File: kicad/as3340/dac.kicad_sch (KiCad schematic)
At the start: 29 parts, among them U14 AD5328, U2 LM4040AIM3-2.5, U5 TL074

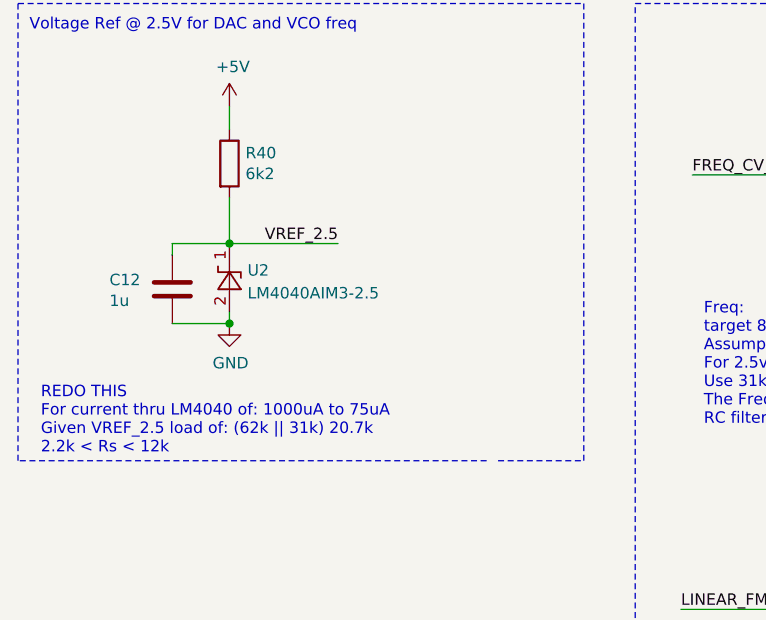
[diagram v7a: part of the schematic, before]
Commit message: some routing modifications and updated JLCPCB parts list
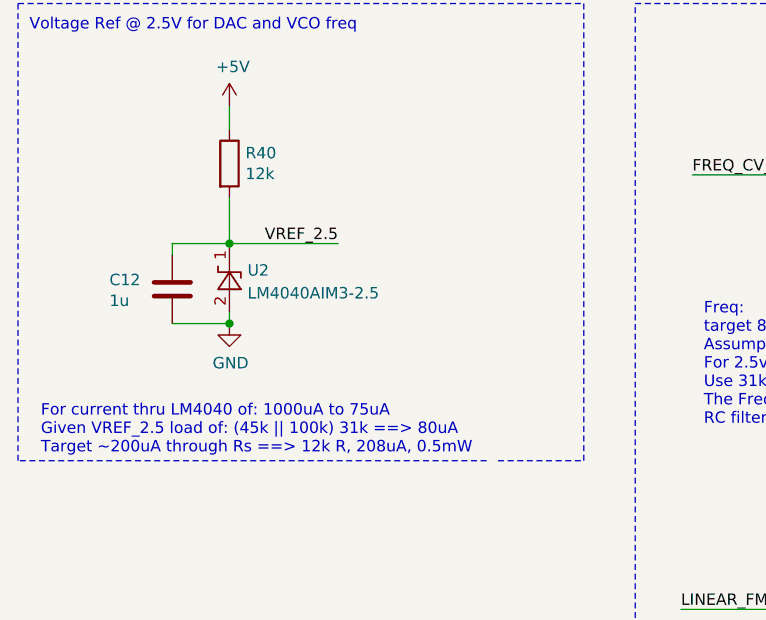
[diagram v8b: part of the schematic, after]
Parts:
- C16: LCSC Part C2761748 -> C21122
- C3: LCSC Part (none) -> C1588
- C36: LCSC Part (none) -> C53987
- R38, R39: LCSC Part (none) -> C25803
- R40: value 6k2 -> 12k; footprint Resistor_SMD:R_1206_3216Metric -> Resistor_SMD:R_0603_1608Metric; LCSC Part (none) -> C22790
- R50: LCSC Part (none) -> C21190
- R61: LCSC Part (none) -> C4216
- R64: LCSC Part (none) -> C23196
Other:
- note added: "For current thru LM4040 of: 1000uA to 75uA Given VREF_2.5 load of: (45k || 100k) 31k ==> 80uA Target ~200uA through Rs ==> 12k R, 208uA, 0.5mW"
- note removed: "REDO THIS For current thru LM4040 of: 1000uA to 75uA Given VREF_2.5 load of: (62k || 31k) 20.7k 2.2k < Rs < 12k"
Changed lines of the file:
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@@
   (title_block
     (title "Zoxnoxious 3340 Oscillator")
-    (rev "0.4")
+    (date "2024-06-20")
+    (rev "0.7")
     (company "Zoxnoxious Engineering")
   )
@@
     (effects (font (size 1.27 1.27)) (justify left bottom))
   )
-  (text "REDO THIS\nFor current thru LM4040 of: 1000uA to 75uA\nGiven VREF_2.5 load of: (62k || 31k) 20.7k\n2.2k < Rs < 12k\n"
+  (text "For current thru LM4040 of: 1000uA to 75uA\nGiven VREF_2.5 load of: (45k || 100k) 31k ==> 80uA\nTarget ~200uA through Rs ==> 12k R, 208uA, 0.5mW\n"
     (at 20.32 168.275 0)
     (effects (font (size 1.27 1.27)) (justify left bottom))
@@
       (effects (font (size 1.27 1.27)) hide)
     )
-    (property "LCSC Part" "" (at 118.11 137.16 0)
+    (property "LCSC Part" "C21190" (at 118.11 137.16 0)
       (effects (font (size 1.27 1.27)) hide)
     )
@@
       (effects (font (size 1.27 1.27)) hide)
     )
-    (property "LCSC Part" "" (at 245.11 58.42 0)
+    (property "LCSC Part" "C4216" (at 245.11 58.42 0)
       (effects (font (size 1.27 1.27)) hide)
     )
@@
       (effects (font (size 1.27 1.27)) hide)
     )
-    (property "LCSC Part" "" (at 261.62 52.07 0)
+    (property "LCSC Part" "C23196" (at 261.62 52.07 0)
       (effects (font (size 1.27 1.27)) hide)
     )
@@
       (effects (font (size 1.27 1.27)) hide)
     )
-    (property "LCSC Part" "" (at 332.74 58.42 0)
+    (property "LCSC Part" "C25803" (at 332.74 58.42 0)
       (effects (font (size 1.27 1.27)) hide)
     )
@@
       (effects (font (size 1.27 1.27)) (justify left))
     )
-    (property "Value" "6k2" (at 43.053 137.033 0)
+    (property "Value" "12k" (at 43.053 137.033 0)
       (effects (font (size 1.27 1.27)) (justify left))
     )
-    (property "Footprint" "Resistor_SMD:R_1206_3216Metric" (at 39.497 135.89 90)
+    (property "Footprint" "Resistor_SMD:R_0603_1608Metric" (at 39.497 135.89 90)
       (effects (font (size 1.27 1.27)) hide)
     )
@@
       (effects (font (size 1.27 1.27)) hide)
     )
-    (property "LCSC Part" "" (at 41.275 135.89 0)
+    (property "LCSC Part" "C22790" (at 41.275 135.89 0)
       (effects (font (size 1.27 1.27)) hide)
     )
@@
       (effects (font (size 1.27 1.27)) hide)
     )
-    (property "LCSC Part" "" (at 349.25 52.07 0)
+    (property "LCSC Part" "C25803" (at 349.25 52.07 0)
       (effects (font (size 1.27 1.27)) hide)
     )
@@
       (effects (font (size 1.27 1.27)) hide)
     )
-    (property "LCSC Part" "" (at 349.25 41.91 0)
+    (property "LCSC Part" "C1588" (at 349.25 41.91 0)
       (effects (font (size 1.27 1.27)) hide)
     )
@@
       (effects (font (size 1.27 1.27)) hide)
     )
-    (property "LCSC Part" "C2761748" (at 128.27 191.77 0)
+    (property "LCSC Part" "C21122" (at 128.27 191.77 0)
       (effects (font (size 1.27 1.27)) hide)
     )
@@
       (effects (font (size 1.27 1.27)) hide)
     )
-    (property "LCSC Part" "" (at 261.62 41.91 0)
-      (effects (font (size 1.27 1.27)) hide)
-    )
+    (property "LCSC Part" "C53987" (at 261.62 41.91 0)
+      (effects (font (size 1.27 1.27)) hide)
+    )
